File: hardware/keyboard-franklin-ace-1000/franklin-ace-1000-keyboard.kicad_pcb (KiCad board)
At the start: 2 copper layers, 410 x 128.5 mm, 158 parts, among them J1 Conn_02x20_Odd_Even, K1 ESC, K10 A, K11 Z, K12 2 @, K13 W, K14 S, K15 X, K16 3 #, K17 E, K18 D, K19 C, K2 BREAK, K20 4 $, K21 R, K22 F, K23 V, K24 5 &, K25 T, K26 G, K27 B, K28 6 ^, K29 Y, K3 PAUSE, K30 H, K31 N, K32 SPACE_8U, K33 7 &, K34 U, K35 J, K36 M, K37 8 *, K38 I, K39 K, K4 CTRL, K40 , <, K41 9 (, K42 O, K43 L, K44 . >, K45 RIGHT, K46 -, K47 +, K48 *, K49 0 ), K5 TAB, K50 P, K51 ; :, K52 / ?, K53 7, K54 4, K55 1, K56 >, K57 - / _, K58 [ {, K59 ; ", K6 LOCK, K60 SHIFT, K61 8, K62 5, K63 2, K64 0, K65 + / =, K66 ] }, K67 RETURN, K68 LEFT, K69 9, K7 SHIFT, K70 6, K71 3, K72 ., K73 SPACE_1U, K8 1 !, K9 Q

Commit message: Updates to Franklin Ace keyboard
- Use the dual footprints for futaba / cherry keys

- include a diode for every key.

- Add stabilizers to the spacebar

- The Franklin keyboard is 9u, but it's very hard to find a 9u option. Instead, use 8u+1u

- Replace the LOCK key with a 1.75U key with LED window. Fix LED spacing to match original.
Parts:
- added D74: diode-combined, unikbd:diode-combined, F.Cu at (154.4, 164.5)
- added K74: TAB2, unikbd:Key_MX, F.Cu at (144.8, 164.1)
- added R2: RES 330 ohm 1% MLCC 0805 Yageo, Resistor_SMD:R_0805_2012Metric, F.Cu at (250.5, 136.8)
- D75, D76, D77, D78, D79, D80, D81, D82: footprint Diode_THT:D_DO-35_SOD27_P7.62mm_Horizontal -> unikbd:diode-combined
- D84: renamed from D74; footprint Diode_THT:D_DO-35_SOD27_P7.62mm_Horizontal -> unikbd:diode-combined
- R1: value R = (Vcc – Vd) / Id -> 330 ohms; moved to B.Cu
- moved D72 423.4 mm to (483.1, 221.7), turned to 90 degrees
- moved D71 421.3 mm to (483.1, 202.5), turned to 90 degrees
- moved D64 412.2 mm to (464.0, 221.7), turned to 90 degrees
- moved D63 408.7 mm to (464.0, 202.5), turned to 90 degrees
- moved D56 397.2 mm to (444.9, 221.7), turned to 90 degrees
- moved D55 394.8 mm to (444.9, 202.5), turned to 90 degrees
- moved D48 387.0 mm to (425.9, 221.7), turned to 90 degrees
- moved D47 383.2 mm to (425.9, 202.5), turned to 90 degrees
- moved D60 355.2 mm to (405.4, 221.6), turned to 90 degrees
- moved D67 344.9 mm to (402.6, 202.6), turned to 90 degrees
- moved D59 327.8 mm to (379.8, 202.5), turned to 90 degrees
- moved D52 327.1 mm to (368.8, 221.5), turned to 90 degrees
- moved D51 313.4 mm to (358.5, 202.5), turned to 90 degrees
- moved D44 311.6 mm to (349.7, 221.5), turned to 90 degrees
- moved D43 299.1 mm to (339.5, 202.5), turned to 90 degrees
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- renumbered D83 to D73, D73 to D83
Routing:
- net Col0: track 1122.8 -> 471.3 mm
- net Row0: track 17.7 -> 430.7 mm, vias 0 -> 4
- net Row6: track 17.3 -> 264.5 mm, vias 0 -> 3
- net Row10: track 0.00 -> 244.0 mm, vias 0 -> 1
- net Row9: track 50.8 -> 285.5 mm
- net (no net): track 233.0 -> 0.00 mm
- net Row7: track 36.7 -> 254.9 mm, vias 0 -> 4
- net Row5: track 36.7 -> 240.0 mm, vias 0 -> 3
- net Row1: track 41.1 -> 235.1 mm, vias 0 -> 1
- net Net-(D7-K): track 207.3 -> 19.9 mm
- net Row2: track 21.6 -> 198.7 mm, vias 0 -> 4
- net Col7: track 601.0 -> 472.1 mm, vias 0 -> 5
- net Row3: track 41.1 -> 166.4 mm, vias 0 -> 3
- net Net-(D81-K): track 137.7 -> 40.1 mm, vias 0 -> 1
- net Row4: track 60.8 -> 152.8 mm, vias 0 -> 3
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
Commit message: Update the keyboard to use project conventions
- Use the dual footprints for futaba / cherry keys
- Include a diode for every key (dual SMT/TH options)
- Add stabilizers to the spacebar
- Add cherry and futaba aligner plates
- Add SMT resistor option
- Add unified retro keyboard text
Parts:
- added REF**: MountingHole_3.2mm_M3, MountingHole:MountingHole_3.2mm_M3, F.Cu at (233.9, 144.0)
- added REF**: MountingHole_3.2mm_M3, MountingHole:MountingHole_3.2mm_M3, F.Cu at (357.5, 144.0)
- added REF**: MountingHole_3.2mm_M3, MountingHole:MountingHole_3.2mm_M3, F.Cu at (167.1, 244.7)
- added REF**: MountingHole_3.2mm_M3, MountingHole:MountingHole_3.2mm_M3, F.Cu at (477.2, 244.7)
- added REF**: MountingHole_3.2mm_M3, MountingHole:MountingHole_3.2mm_M3, F.Cu at (118.0, 144.0)
- added REF**: MountingHole_3.2mm_M3, MountingHole:MountingHole_3.2mm_M3, F.Cu at (381.1, 244.7)
- added REF**: MountingHole_3.2mm_M3, MountingHole:MountingHole_3.2mm_M3, F.Cu at (119.9, 244.7)
- added REF**: MountingHole_3.2mm_M3, MountingHole:MountingHole_3.2mm_M3, F.Cu at (477.2, 144.0)
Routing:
- net Col7: track 472.1 -> 469.5 mm
- net Col6: track 646.5 -> 648.8 mm
- net Row1: track 235.1 -> 232.9 mm
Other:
- board text added: "${TITLE} ${COMPANY} Rev ${REVISION} ${ISSUE_DATE} ${COMMENT1} ${COMMENT2}"
- board text removed: "Franklin ACE 1000 Keyboard (for use with Unified Retro Keyboard ASCII Interface) v0.9 2023 竜 クリストファー (Chris Ryu)"

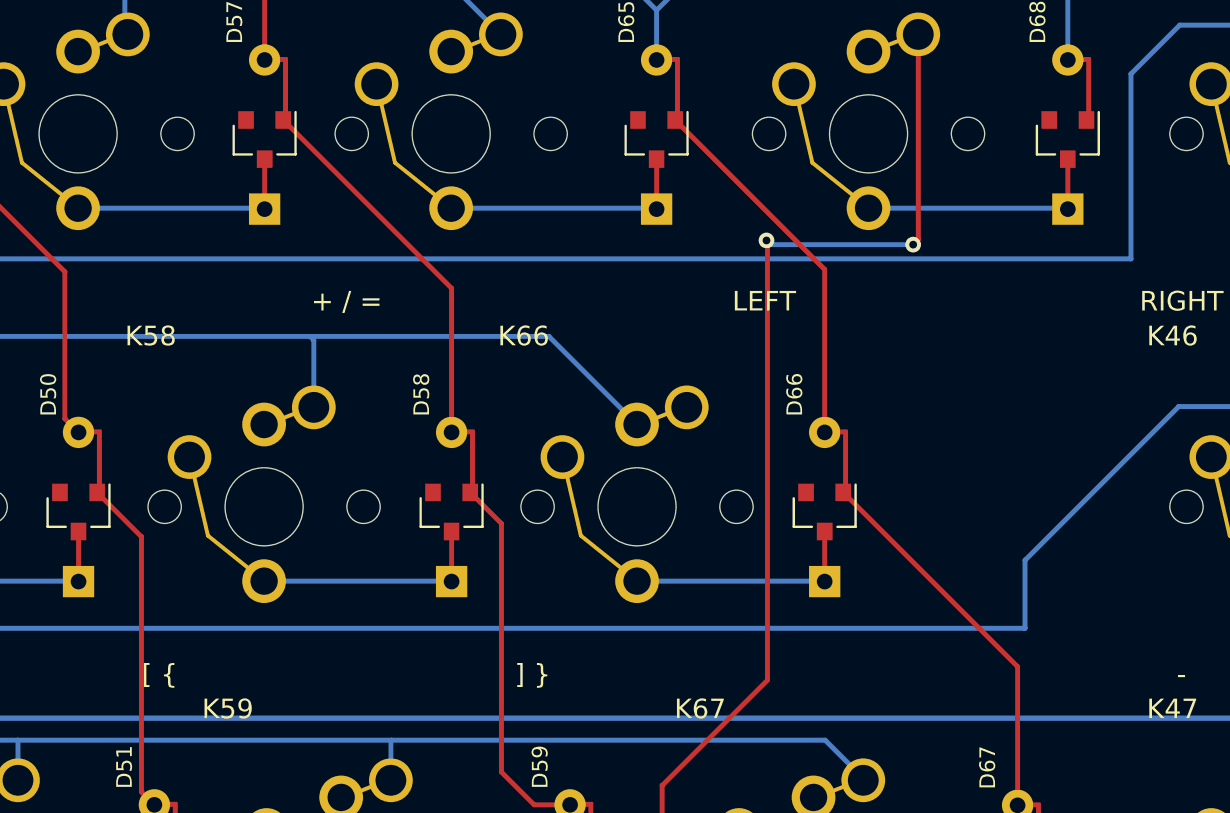
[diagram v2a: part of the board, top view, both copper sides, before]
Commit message: Moved some keys to better position
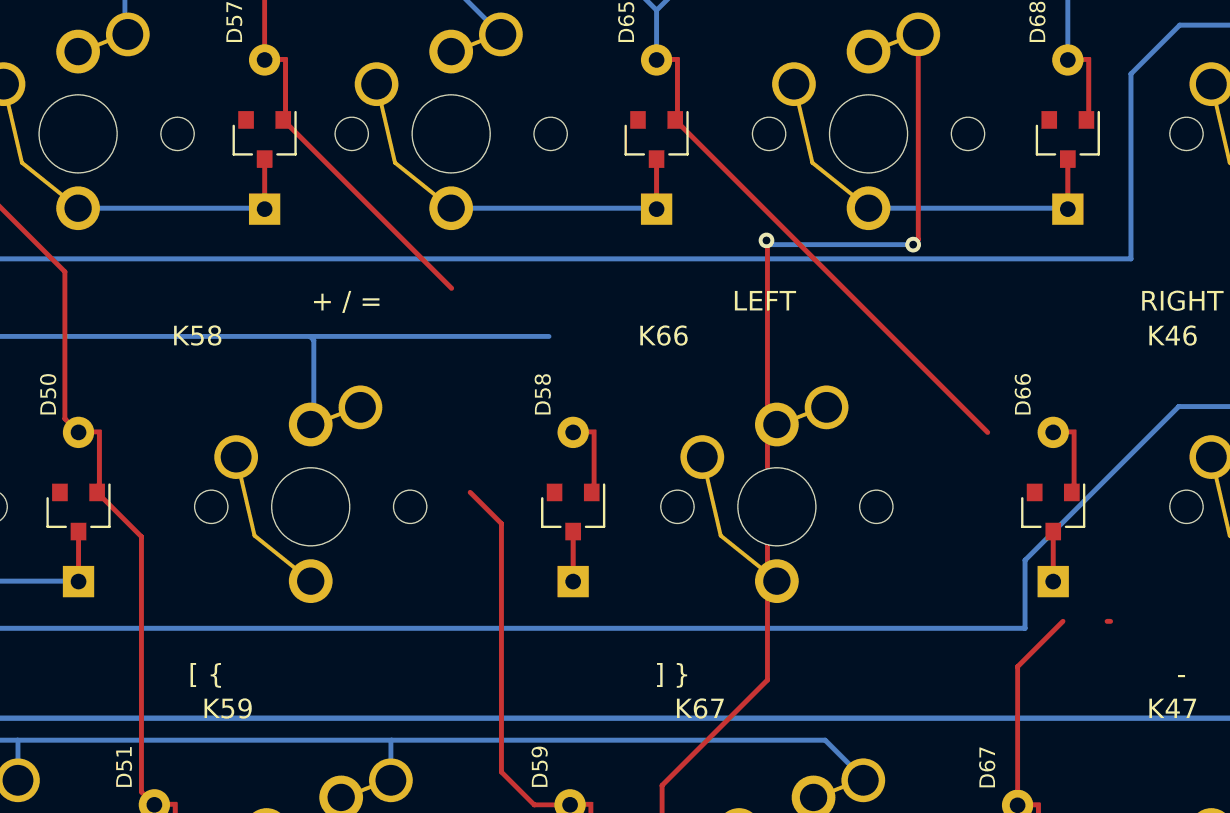
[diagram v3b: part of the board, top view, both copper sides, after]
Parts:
- moved D66 11.7 mm to (404.5, 183.5)
- moved K66 7.14 mm to (390.3, 183.2)
- moved D58 6.21 mm to (379.9, 183.5)
- moved K58 2.38 mm to (366.5, 183.2)
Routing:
- net Net-(D66-K): track 9.56 -> 0.00 mm
- net Net-(D58-K): track 9.56 -> 0.00 mm
- net Row7: track 254.9 -> 247.5 mm
- net Col1: track 400.3 -> 394.0 mm
- net Row9: track 285.5 -> 279.8 mm
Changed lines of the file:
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@@
   )
   (footprint "unikbd:Key_MX" locked (layer "F.Cu")
-    (at 364.151036 183.150352)
+    (at 366.532286 183.150352)
     (property "Sheetfile" "franklin-ace-1000-keyboard.kicad_sch")
     (property "Sheetname" "")
@@
   )
   (footprint "unikbd:Key_MX" locked (layer "F.Cu")
-    (at 383.201036 183.150352)
+    (at 390.344786 183.150352)
     (property "Sheetfile" "franklin-ace-1000-keyboard.kicad_sch")
     (property "Sheetname" "")
@@
   )
   (footprint "unikbd:diode-combined" locked (layer "F.Cu")
-    (at 373.72867 183.515 90)
+    (at 379.938971 183.515 90)
     (descr "Diode, DO-35_SOD27 series, Axial, Horizontal, pin pitch=7.62mm, , length*diameter=4*2mm^2, , http://www.diodes.com/_files/packages/DO-35.pdf")
     (tags "Diode DO-35_SOD27 series Axial Horizontal pin pitch 7.62mm  length 4mm diameter 2mm")
@@
   )
   (footprint "unikbd:diode-combined" locked (layer "F.Cu")
-    (at 392.7856 183.515 90)
+    (at 404.46031 183.515 90)
     (descr "Diode, DO-35_SOD27 series, Axial, Horizontal, pin pitch=7.62mm, , length*diameter=4*2mm^2, , http://www.diodes.com/_files/packages/DO-35.pdf")
     (tags "Diode DO-35_SOD27 series Axial Horizontal pin pitch 7.62mm  length 4mm diameter 2mm")
@@
   (segment (start 164.126036 167.999252) (end 173.536452 167.999252) (width 0.254) (layer "B.Cu") (net 8))
   (segment (start 173.524036 187.049252) (end 183.137652 187.049252) (width 0.254) (layer "B.Cu") (net 9))
-  (segment (start 402.6408 191.4202) (end 393.7356 182.515) (width 0.25) (layer "F.Cu") (net 10))
   (segment (start 483.0318 160.4264) (end 481.8888 160.4264) (width 0.254) (layer "F.Cu") (net 10))
+  (segment (start 402.6408 191.4202) (end 404.958 189.103) (width 0.25) (layer "F.Cu") (net 10))
+  (segment (start 385.1504 163.4904) (end 401.111 179.451) (width 0.254) (layer "F.Cu") (net 10))
   (segment (start 483.1334 198.4756) (end 484.9368 196.6722) (width 0.25) (layer "F.Cu") (net 10))
+  (segment (start 402.6408 198.501) (end 402.6408 191.4202) (width 0.25) (layer "F.Cu") (net 10))
   (segment (start 480.695 174.7774) (end 483.0318 177.1142) (width 0.254) (layer "F.Cu") (net 10))
   (segment (start 485.2924 208.7118) (end 485.2924 202.7486) (width 0.25) (layer "F.Cu") (net 10))
   (segment (start 483.1334 217.678) (end 483.1334 210.8708) (width 0.25) (layer "F.Cu") (net 10))
-  (segment (start 392.7856 171.1256) (end 392.7856 179.451) (width 0.254) (layer "F.Cu") (net 10))
   (segment (start 484.9368 183.3684) (end 484.0834 182.515) (width 0.25) (layer "F.Cu") (net 10))
-  (segment (start 402.6408 198.501) (end 402.6408 191.4202) (width 0.25) (layer "F.Cu") (net 10))
   (segment (start 480.695 161.6202) (end 480.695 174.7774) (width 0.254) (layer "F.Cu") (net 10))
   (segment (start 483.0318 177.1142) (end 483.0318 179.451) (width 0.254) (layer "F.Cu") (net 10))
+  (segment (start 407.2128 189.103) (end 407.3906 189.103) (width 0.25) (layer "F.Cu") (net 10))
   (segment (start 485.2924 202.7486) (end 484.0834 201.5396) (width 0.25) (layer "F.Cu") (net 10))
-  (segment (start 385.1504 163.4904) (end 392.7856 171.1256) (width 0.254) (layer "F.Cu") (net 10))
   (segment (start 483.1334 210.8708) (end 485.2924 208.7118) (width 0.25) (layer "F.Cu") (net 10))
   (segment (start 484.9368 196.6722) (end 484.9368 183.3684) (width 0.25) (layer "F.Cu") (net 10))
@@
   (segment (start 328.591036 178.171952) (end 328.591036 174.558116) (width 0.25) (layer "B.Cu") (net 23))
   (segment (start 366.4966 174.549352) (end 378.702136 174.549352) (width 0.25) (layer "B.Cu") (net 23))
-  (segment (start 378.702136 174.549352) (end 383.201036 179.048252) (width 0.25) (layer "B.Cu") (net 23))
   (segment (start 366.691036 178.171952) (end 366.691036 174.743788) (width 0.25) (layer "B.Cu") (net 23))
   (segment (start 176.064036 178.171952) (end 179.186636 175.049352) (width 0.254) (layer "B.Cu") (net 23))
@@
   (segment (start 435.398036 225.276252) (end 444.926985 225.276252) (width 0.25) (layer "B.Cu") (net 87))
   (segment (start 354.649797 167.999252) (end 364.105712 167.999252) (width 0.254) (layer "B.Cu") (net 88))
-  (segment (start 364.151036 187.049252) (end 373.706922 187.049252) (width 0.254) (layer "B.Cu") (net 89))
   (segment (start 368.088036 206.099252) (end 379.777148 206.099252) (width 0.25) (layer "B.Cu") (net 90))
   (segment (start 387.773036 225.149252) (end 405.431148 225.149252) (width 0.25) (layer "B.Cu") (net 91))
@@
   (segment (start 454.448036 225.276252) (end 464.019318 225.276252) (width 0.25) (layer "B.Cu") (net 95))
   (segment (start 373.706723 167.999252) (end 384.153252 167.999252) (width 0.254) (layer "B.Cu") (net 96))
-  (segment (start 383.201036 187.049252) (end 392.763852 187.049252) (width 0.254) (layer "B.Cu") (net 97))
   (segment (start 392.218036 206.099252) (end 402.619052 206.099252) (width 0.25) (layer "B.Cu") (net 98))
   (segment (start 394.885036 167.999252) (end 405.159052 167.999252) (width 0.254) (layer "B.Cu") (net 99))
@@
   (segment (start 383.2352 207.6958) (end 383.2352 204.044) (width 0.25) (layer "F.Cu") (net 122))
   (segment (start 374.67867 182.515) (end 376.2756 184.11193) (width 0.25) (layer "F.Cu") (net 122))
-  (segment (start 373.72867 172.09081) (end 373.72867 179.451) (width 0.254) (layer "F.Cu") (net 122))
   (segment (start 464.041066 209.820934) (end 465.8868 207.9752) (width 0.25) (layer "F.Cu") (net 122))
   (segment (start 465.8868 202.4946) (end 464.9318 201.5396) (width 0.25) (layer "F.Cu") (net 122))

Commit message: More key fixes
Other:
- board text added: "Keyboard cutout on User ECO 1 layer."

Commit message: True up Franklin 1000 key spacing
- Make sure each 1U is 0.75 inch.
- Record key width for all keys > 1U, and ensure spacing is correct.
- create symbols for the mx keys
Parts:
- K58: value [ { -> { }
- K60: value SHIFT -> R SHIFT
- K66: value ] } -> [ ]
- K7: value SHIFT -> L SHIFT
- moved K58 2.89 mm to (363.6, 183.2)
- moved D2 2.27 mm to (137.4, 183.5)
- moved D67 1.48 mm to (404.1, 202.6)
- moved D6 0.56 mm to (141.5, 202.5)
- moved D50 0.55 mm to (354.1, 183.5)
- moved K65 0.54 mm to (373.2, 164.1)
- moved D57 0.54 mm to (363.6, 164.5)
- moved K57 0.53 mm to (354.1, 164.1)
- moved D59 0.53 mm to (380.3, 202.5)
- moved D49 0.53 mm to (344.6, 164.5)
- moved K49 0.52 mm to (335.1, 164.1)
- moved D41 0.52 mm to (325.5, 164.5)
- moved K41 0.52 mm to (316.0, 164.1)
- moved D37 0.51 mm to (306.5, 164.5)
- moved K37 0.51 mm to (297.0, 164.1)
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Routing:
- net Net-(D58-K): track 0.00 -> 16.3 mm
- net Net-(D66-K): track 0.00 -> 14.1 mm
- net Row9: track 279.8 -> 290.0 mm
- net Row7: track 247.5 -> 257.5 mm
- net Col3: track 473.9 -> 483.3 mm
- net Col1: track 394.0 -> 389.4 mm, vias 3 -> 5
- net Col5: track 444.9 -> 448.7 mm
- net Row0: track 430.4 -> 427.0 mm
- net Net-(D2-K): track 9.28 -> 12.0 mm
- net Net-(D67-K): track 10.4 -> 11.9 mm
- net Col4: track 439.6 -> 440.7 mm
